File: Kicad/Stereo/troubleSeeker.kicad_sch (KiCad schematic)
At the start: 19 parts, among them J1 Screw_Terminal_01x02, J2 AudioJack2, SW1 SW_DPST_x2, U1 TL072

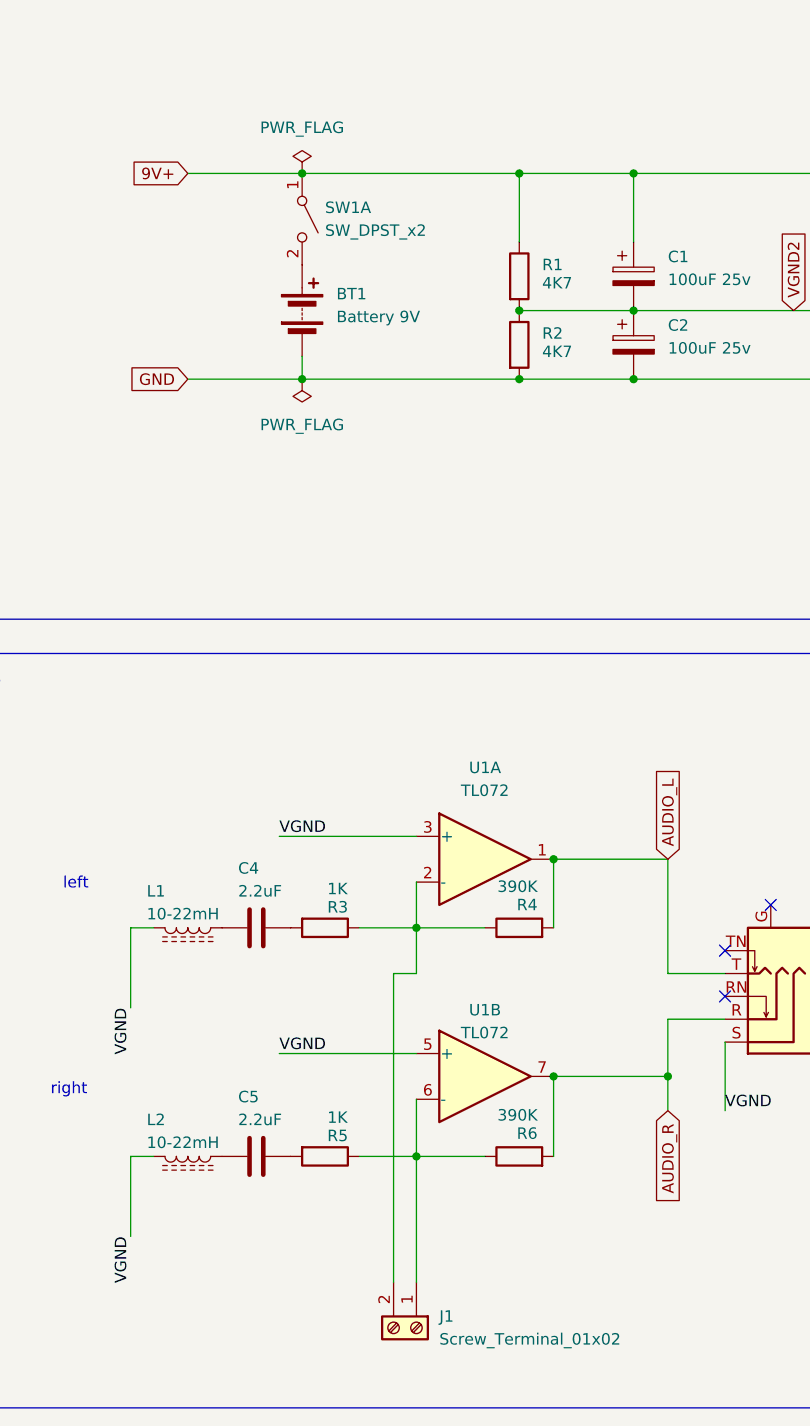
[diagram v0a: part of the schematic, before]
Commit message: Replaced switch
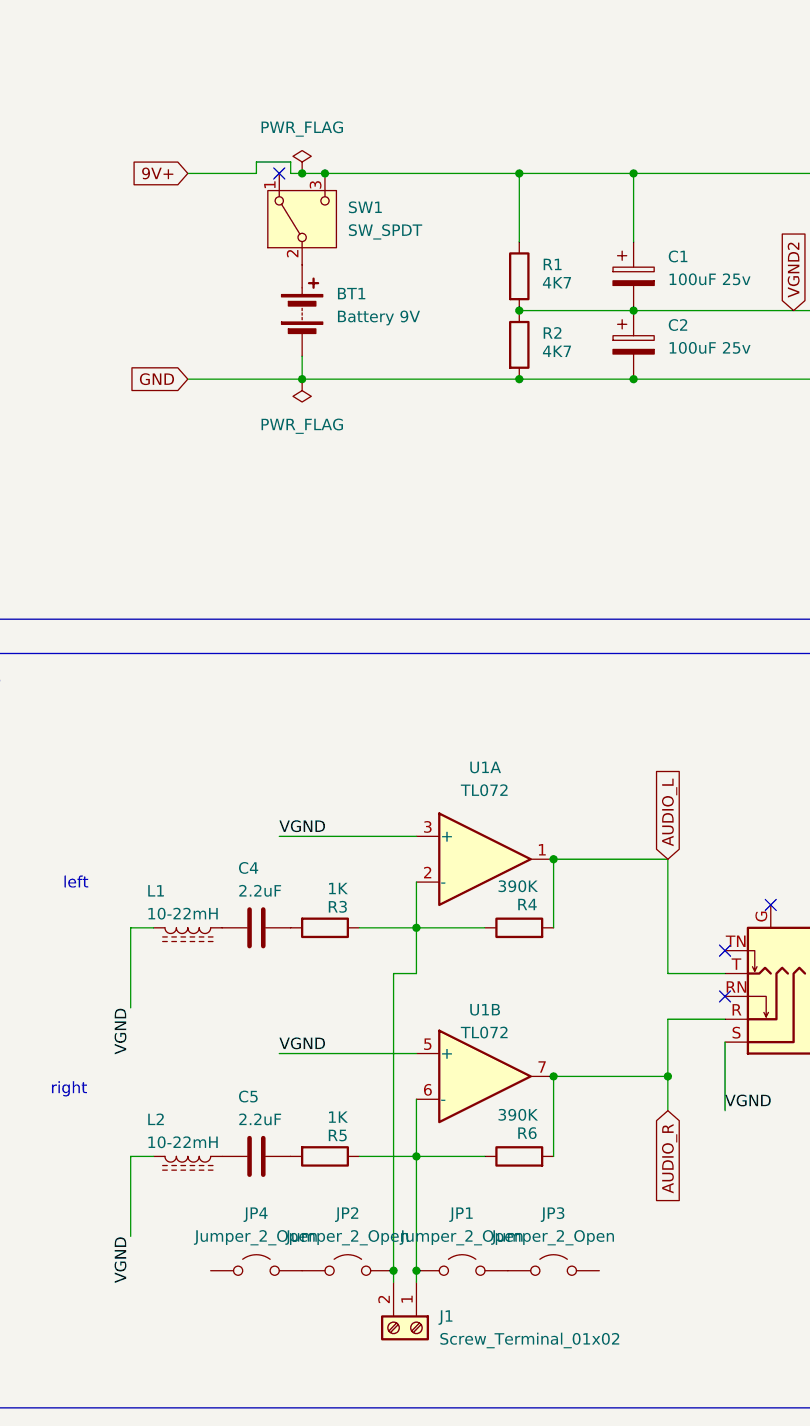
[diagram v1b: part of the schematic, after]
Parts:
- removed SW1: SW_DPST_x2, Button_Switch_THT:SW_Push_2P1T_Toggle_CK_PVA1xxH1xxxxxxV2, symbol Switch:SW_DPST_x2
- added JP1, JP2, JP3, JP4: Jumper_2_Open, Jumper:SolderJumper-2_P1.3mm_Open_RoundedPad1.0x1.5mm, symbol Jumper:Jumper_2_Open
- added SW1: SW_SPDT, Button_Switch_THT:SW_Slide_SPDT_Angled_CK_OS102011MA1Q, symbol Switch:SW_SPDT
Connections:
- net 4.5V: now also SW1.3 (C)
- net at J1.1 (Pin_1), R5.1, R6.1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: now also JP1.1 (A)
- net at J1.2 (Pin_2), R3.1, R4.1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: now also JP2.2 (B)
- net at BT1.1 (+): now also SW1.2 (B)
- new net: JP1.2 (B), JP3.1 (A)
- new net: JP2.1 (A), JP4.2 (B)
- no-connect marks 8 -> 9
